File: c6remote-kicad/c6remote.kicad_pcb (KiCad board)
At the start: 2 copper layers, 37 x 130 mm, 46 parts, among them J1 Battery, Q1 MMBT2222A, SW1 SW_Push, SW10 SW_Push, SW11 SW_Push, SW2 SW_Push, SW3 SW_Push, SW4 SW_Push, SW5 SW_Push, SW6 SW_Push, SW7 SW_Push, SW8 SW_Push, SW9 SW_Push, U1 XIAO-ESP32-C6, U2 TSOP4136, U3 PCF8575DBR

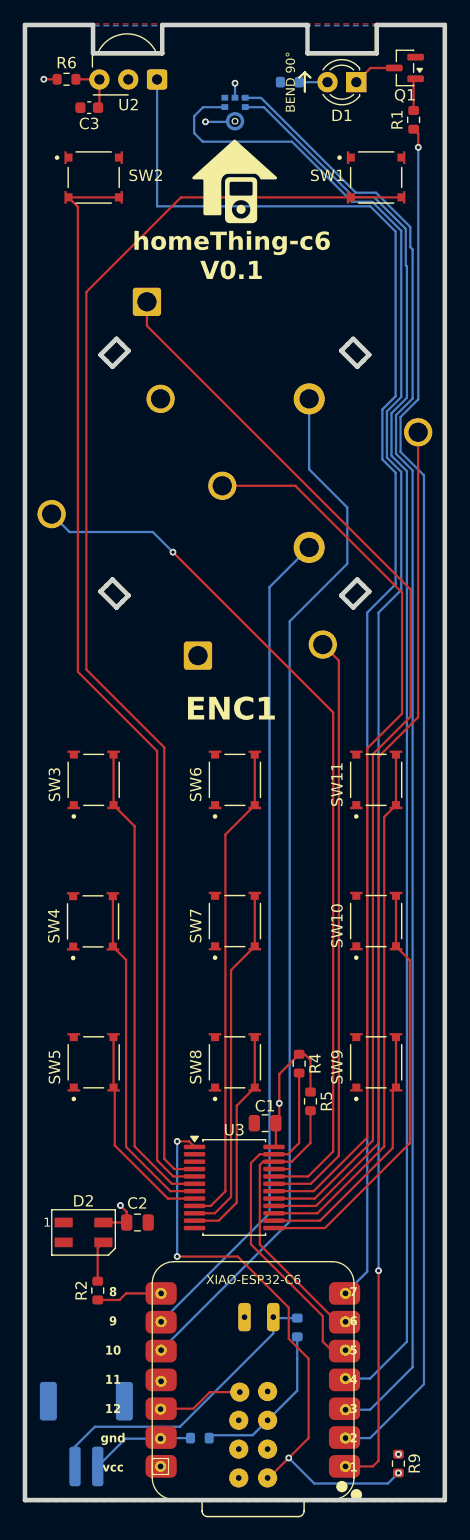
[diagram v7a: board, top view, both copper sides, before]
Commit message: fix(pcb): move IR receiver U2 to back side (B.Cu) for tall-part clearance, clean up silk and orphaned +3.3V via - relocated U2 to bottom, deleted dangling +3.3V via at (51,33), reduced silk overlaps; DRC 0 errors unconnected 0 parity 13, 41 remaining silk/lib warnings
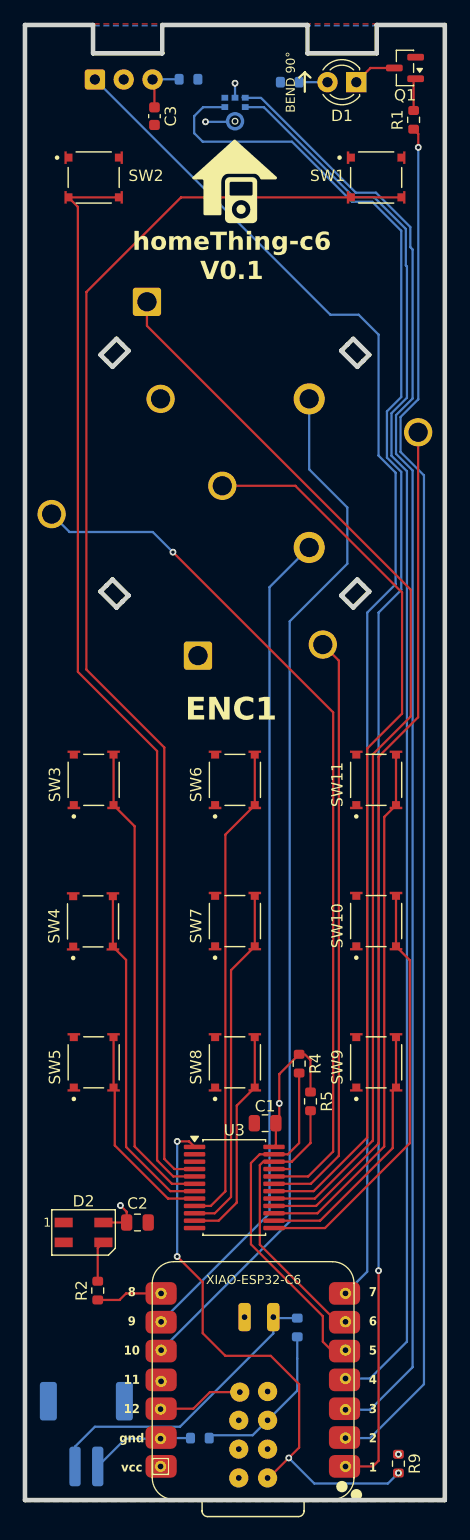
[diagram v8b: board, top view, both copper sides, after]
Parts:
- R6, U2: moved to B.Cu
- moved R6 10.8 mm to (49.2, 33.0), turned to 180 degrees
- moved C3 5.80 mm to (46.2, 36.2), turned to -90 degrees
- moved U2 5.48 mm to (41.0, 33.0), turned to 0 degrees
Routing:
- net IR REC: track 129.5 -> 121.3 mm
- net exp_int: track 52.1 -> 50.6 mm
- net +3.3V: track 25.5 -> 24.3 mm, vias 4 -> 3
